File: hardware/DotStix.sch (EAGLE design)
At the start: 22 parts, among them U1 ATMEGA328P-MU-QFN32

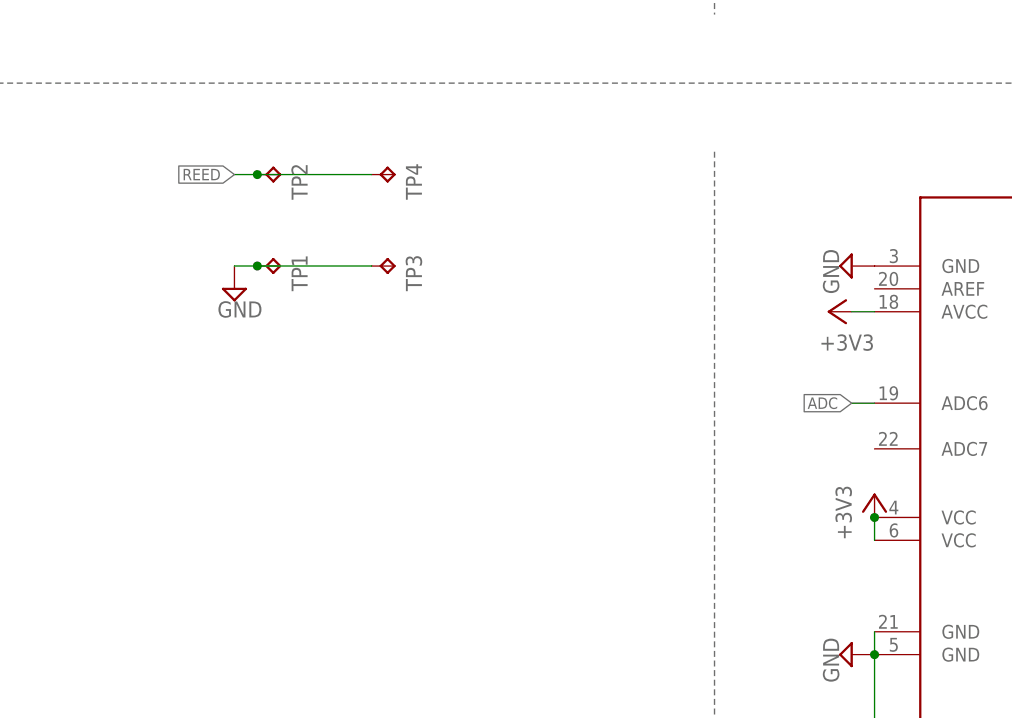
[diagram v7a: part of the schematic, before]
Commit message: Add weak pullup for low current with battery
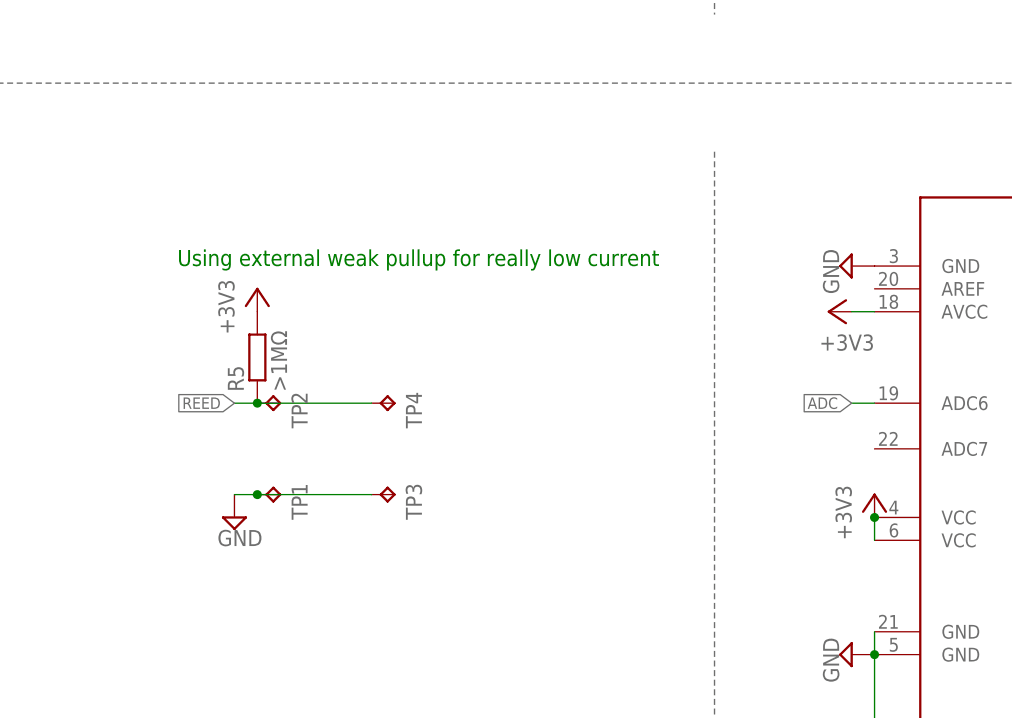
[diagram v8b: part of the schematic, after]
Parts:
- added R5: >1MΩ, resistor:R-EU_R0603
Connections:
- net +3V3: now also R5.2
- net REED: now also R5.1
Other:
- note added: "Using external weak pullup for really low current"
- moved on the sheet: TP1, TP2, TP3, TP4
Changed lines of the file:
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@@
 <part name="C9" library="rcl" deviceset="C-EU" device="C0603" value="7pF"/>
 <part name="SUPPLY26" library="supply2" deviceset="GND" device=""/>
+<part name="R5" library="resistor" deviceset="R-EU_" device="R0603" value="&gt;1MΩ"/>
+<part name="+3V8" library="supply1" deviceset="+3V3" device=""/>
 </parts>
 <sheets>
@@
 <wire x1="312.42" y1="190.5" x2="312.42" y2="109.22" width="0.1524" layer="95" style="longdash"/>
 <text x="364.49" y="163.83" size="1.778" layer="91">Sensor</text>
+<text x="69.85" y="81.28" size="1.778" layer="91">Using external weak pullup for really low current</text>
 </plain>
 <instances>
@@
 <instance part="+3V7" gate="G$1" x="2.54" y="74.93" rot="R90"/>
 <instance part="SUPPLY2" gate="GND" x="11.43" y="69.85"/>
-<instance part="TP1" gate="G$1" x="81.28" y="81.28" rot="R270"/>
-<instance part="TP2" gate="G$1" x="81.28" y="91.44" rot="R270"/>
-<instance part="SUPPLY5" gate="GND" x="76.2" y="78.74"/>
+<instance part="TP1" gate="G$1" x="81.28" y="55.88" rot="R270"/>
+<instance part="TP2" gate="G$1" x="81.28" y="66.04" rot="R270"/>
+<instance part="SUPPLY5" gate="GND" x="76.2" y="53.34"/>
 <instance part="U$3" gate="G$1" x="78.74" y="154.94"/>
 <instance part="SUPPLY7" gate="GND" x="83.82" y="152.4"/>
@@
 <instance part="+3V9" gate="G$1" x="36.83" y="53.34"/>
 <instance part="SUPPLY10" gate="GND" x="1.27" y="31.75"/>
-<instance part="TP3" gate="G$1" x="93.98" y="81.28" rot="R270"/>
-<instance part="TP4" gate="G$1" x="93.98" y="91.44" rot="R270"/>
+<instance part="TP3" gate="G$1" x="93.98" y="55.88" rot="R270"/>
+<instance part="TP4" gate="G$1" x="93.98" y="66.04" rot="R270"/>
 <instance part="R3" gate="G$1" x="361.95" y="163.83" rot="R90"/>
 <instance part="R4" gate="G$1" x="361.95" y="153.67" rot="R90"/>
@@
 <instance part="C9" gate="G$1" x="353.06" y="53.34" rot="R90"/>
 <instance part="SUPPLY26" gate="GND" x="368.3" y="43.18"/>
+<instance part="R5" gate="G$1" x="78.74" y="71.12" rot="R90"/>
+<instance part="+3V8" gate="G$1" x="78.74" y="78.74"/>
 </instances>
 <busses>
@@
 <pinref part="TP1" gate="G$1" pin="TP"/>
 <pinref part="SUPPLY5" gate="GND" pin="GND"/>
-<wire x1="78.74" y1="81.28" x2="76.2" y2="81.28" width="0.1524" layer="91"/>
+<wire x1="78.74" y1="55.88" x2="76.2" y2="55.88" width="0.1524" layer="91"/>
 <pinref part="TP3" gate="G$1" pin="TP"/>
-<wire x1="91.44" y1="81.28" x2="78.74" y2="81.28" width="0.1524" layer="91"/>
-<junction x="78.74" y="81.28"/>
+<wire x1="91.44" y1="55.88" x2="78.74" y2="55.88" width="0.1524" layer="91"/>
+<junction x="78.74" y="55.88"/>
 </segment>
 <segment>
@@
 <wire x1="36.83" y1="50.8" x2="36.83" y2="45.72" width="0.1524" layer="91"/>
 </segment>
+<segment>
+<pinref part="R5" gate="G$1" pin="2"/>
+<pinref part="+3V8" gate="G$1" pin="+3V3"/>
+</segment>
 </net>
 <net name="MOSI" class="0">
@@
 <pinref part="TP4" gate="G$1" pin="TP"/>
 <pinref part="TP2" gate="G$1" pin="TP"/>
-<wire x1="78.74" y1="91.44" x2="76.2" y2="91.44" width="0.1524" layer="91"/>
-<label x="76.2" y="91.44" size="1.27" layer="95" rot="R180" xref="yes"/>
-<wire x1="91.44" y1="91.44" x2="78.74" y2="91.44" width="0.1524" layer="91"/>
-<junction x="78.74" y="91.44"/>
-</segment>
-<segment>
+<wire x1="78.74" y1="66.04" x2="76.2" y2="66.04" width="0.1524" layer="91"/>
+<label x="76.2" y="66.04" size="1.27" layer="95" rot="R180" xref="yes"/>
+<wire x1="91.44" y1="66.04" x2="78.74" y2="66.04" width="0.1524" layer="91"/>
+<junction x="78.74" y="66.04"/>
+<pinref part="R5" gate="G$1" pin="1"/>
+</segment>
+<segment>
